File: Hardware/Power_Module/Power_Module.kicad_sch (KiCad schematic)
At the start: 0 parts

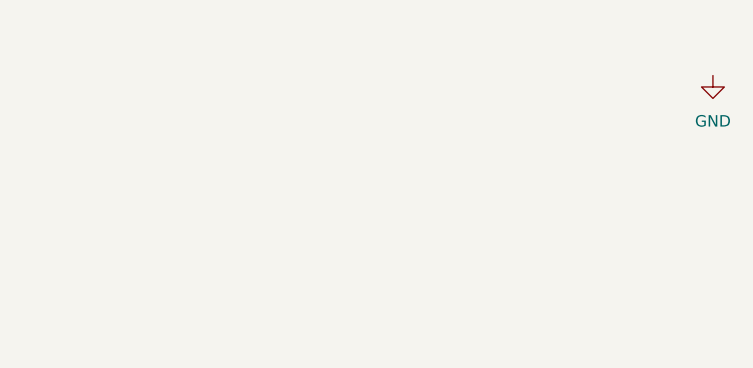
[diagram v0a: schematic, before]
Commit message: added powermodule ic
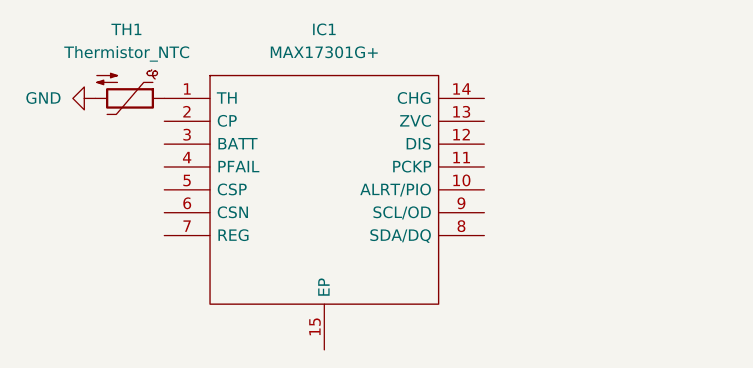
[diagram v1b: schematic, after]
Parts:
- added IC1: MAX17301G+, SON40P300X300X80-15N, symbol MAX17301G+:MAX17301G+
- added TH1: Thermistor_NTC, symbol Device:Thermistor_NTC
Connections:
- net GND: now also TH1.2
- new net: IC1.1 (TH), TH1.1
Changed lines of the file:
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@@
 (kicad_sch
-	(version 20231120)
+	(version 20250114)
 	(generator "eeschema")
-	(generator_version "8.0")
+	(generator_version "9.0")
 	(paper "A4")
 	(symbol
+		(lib_id "MAX17301G+:MAX17301G+")
+		(at 133.35 100.33 0)
+		(unit 1)
+		(exclude_from_sim no)
+		(in_bom yes)
+		(on_board yes)
+		(dnp no)
+		(fields_autoplaced yes)
+		(property "Reference" "IC1"
+			(at 151.13 92.71 0)
+			(effects
+				(font
+					(size 1.27 1.27)
+				)
+			)
+		)
+		(property "Value" "MAX17301G+"
+			(at 151.13 95.25 0)
+			(effects
+				(font
+					(size 1.27 1.27)
+				)
+			)
+		)
+		(property "Footprint" "SON40P300X300X80-15N"
+			(at 165.1 97.79 0)
+			(effects
+				(font
+					(size 1.27 1.27)
+				)
+				(justify left)
+				(hide yes)
+			)
+		)
+		(property "Datasheet" "https://www.analog.com/MAX17301/datasheet"
+			(at 165.1 100.33 0)
+			(effects
+				(font
+					(size 1.27 1.27)
+				)
+				(justify left)
+				(hide yes)
+			)
+		)
+		(property "Description" "1-Cell ModelGauge m5 EZ Fuel Gauge with Protector, Internal Self-Discharge Detection and SHA-256 Authentication"
+			(at 133.35 100.33 0)
+			(effects
+				(font
+					(size 1.27 1.27)
+				)
+				(hide yes)
+			)
+		)
+		(property "Description_1" "1-Cell ModelGauge m5 EZ Fuel Gauge with Protector, Internal Self-Discharge Detection and SHA-256 Authentication"
+			(at 165.1 102.87 0)
+			(effects
+				(font
+					(size 1.27 1.27)
+				)
+				(justify left)
+				(hide yes)
+			)
+		)
+		(property "Height" "0.8"
+			(at 165.1 105.41 0)
+			(effects
+				(font
+					(size 1.27 1.27)
+				)
+				(justify left)
+				(hide yes)
+			)
+		)
+		(property "Mouser Part Number" "700-MAX17301G+"
+			(at 165.1 107.95 0)
+			(effects
+				(font
+					(size 1.27 1.27)
+				)
+				(justify left)
+				(hide yes)
+			)
+		)
+		(property "Mouser Price/Stock" "https://www.mouser.co.uk/ProductDetail/Analog-Devices-Maxim-Integrated/MAX17301G%2b?qs=Wj%2FVkw3K%252BMADpZZVIAh9Qg%3D%3D"
+			(at 165.1 110.49 0)
+			(effects
+				(font
+					(size 1.27 1.27)
+				)
+				(justify left)
+				(hide yes)
+			)
+		)
+		(property "Manufacturer_Name" "Analog Devices"
+			(at 165.1 113.03 0)
+			(effects
+				(font
+					(size 1.27 1.27)
+				)
+				(justify left)
+				(hide yes)
+			)
+		)
+		(property "Manufacturer_Part_Number" "MAX17301G+"
+			(at 165.1 115.57 0)
+			(effects
+				(font
+					(size 1.27 1.27)
+				)
+				(justify left)
+				(hide yes)
+			)
+		)
+		(pin "6"
+		)
+		(pin "5"
+		)
+		(pin "15"
+		)
+		(pin "2"
+		)
+		(pin "13"
+		)
+		(pin "10"
+		)
+		(pin "12"
+		)
+		(pin "7"
+		)
+		(pin "9"
+		)
+		(pin "3"
+		)
+		(pin "14"
+		)
+		(pin "4"
+		)
+		(pin "8"
+		)
+		(pin "1"
+		)
+		(pin "11"
+		)
+		(instances
+			(project ""
+				(path "/48054948-0b09-404e-8bb9-61684bc2977f"
+					(reference "IC1")
+					(unit 1)
+				)
+			)
+		)
+	)
+	(symbol
 		(lib_id "power:GND")
-		(at 194.31 97.79 0)
+		(at 125.73 100.33 270)
 		(unit 1)
 		(exclude_from_sim no)
@@
 		(fields_autoplaced yes)
 		(property "Reference" "#PWR01"
-			(at 194.31 104.14 0)
+			(at 119.38 100.33 0)
 			(effects
 				(font
@@
 		)
 		(property "Value" "GND"
-			(at 194.31 102.87 0)
-			(effects
-				(font
-					(size 1.27 1.27)
-				)
+			(at 121.92 100.3299 90)
+			(effects
+				(font
+					(size 1.27 1.27)
+				)
+				(justify right)
 			)
 		)
 		(property "Footprint" ""
-			(at 194.31 97.79 0)
+			(at 125.73 100.33 0)
 			(effects
 				(font
@@
 		)
 		(property "Datasheet" ""
-			(at 194.31 97.79 0)
+			(at 125.73 100.33 0)
 			(effects
 				(font
@@
 		)
 		(property "Description" "Power symbol creates a global label with name \"GND\" , ground"
-			(at 194.31 97.79 0)
+			(at 125.73 100.33 0)
 			(effects
 				(font
@@
 		)
 	)
+	(symbol
+		(lib_id "Device:Thermistor_NTC")
+		(at 129.54 100.33 270)
+		(unit 1)
+		(exclude_from_sim no)
+		(in_bom yes)
+		(on_board yes)
+		(dnp no)
+		(fields_autoplaced yes)
+		(property "Reference" "TH1"
+			(at 129.2225 92.71 90)
+			(effects
+				(font
+					(size 1.27 1.27)
+				)
+			)
+		)
+		(property "Value" "Thermistor_NTC"
+			(at 129.2225 95.25 90)
+			(effects
+				(font
+					(size 1.27 1.27)
+				)
+			)
+		)
+		(property "Footprint" ""
+			(at 130.81 100.33 0)
+			(effects
+				(font
+					(size 1.27 1.27)
+				)
+				(hide yes)
+			)
+		)
+		(property "Datasheet" "~"
+			(at 130.81 100.33 0)
+			(effects
+				(font
+					(size 1.27 1.27)
+				)
+				(hide yes)
+			)
+		)
+		(property "Description" "Temperature dependent resistor, negative temperature coefficient"
+			(at 129.54 100.33 0)
+			(effects
+				(font
+					(size 1.27 1.27)
+				)
+				(hide yes)
+			)
+		)
+		(pin "1"
+		)
+		(pin "2"
+		)
+		(instances
+			(project ""
+				(path "/48054948-0b09-404e-8bb9-61684bc2977f"
+					(reference "TH1")
+					(unit 1)
+				)
+			)
+		)
+	)
 	(sheet_instances
 		(path "/"
@@
 		)
 	)
+	(embedded_fonts no)
 )

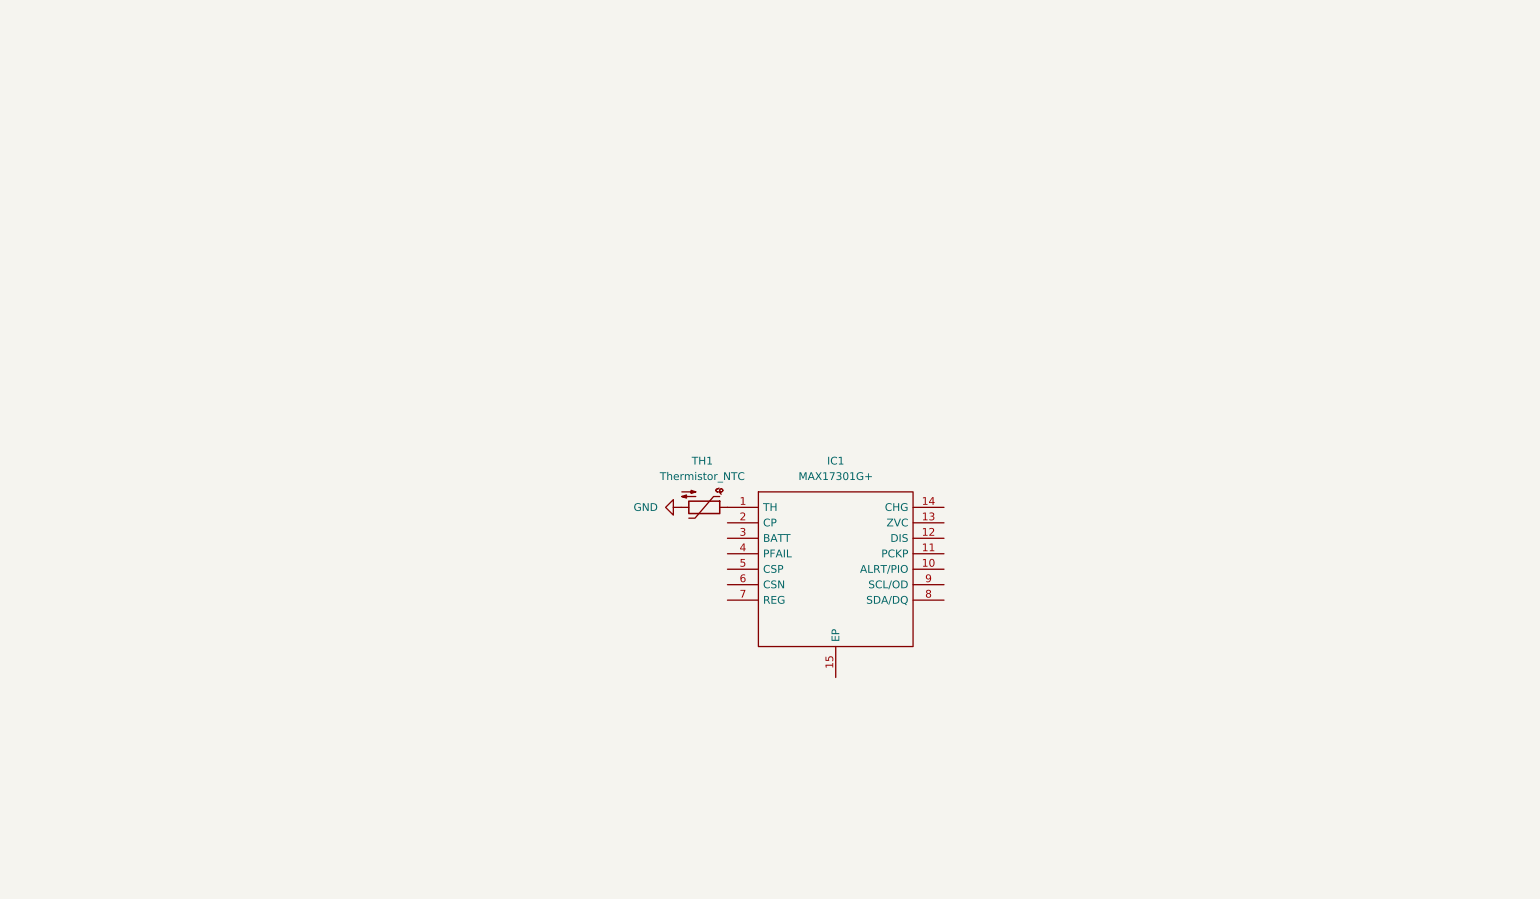
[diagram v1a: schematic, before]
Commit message: Added power module pcb
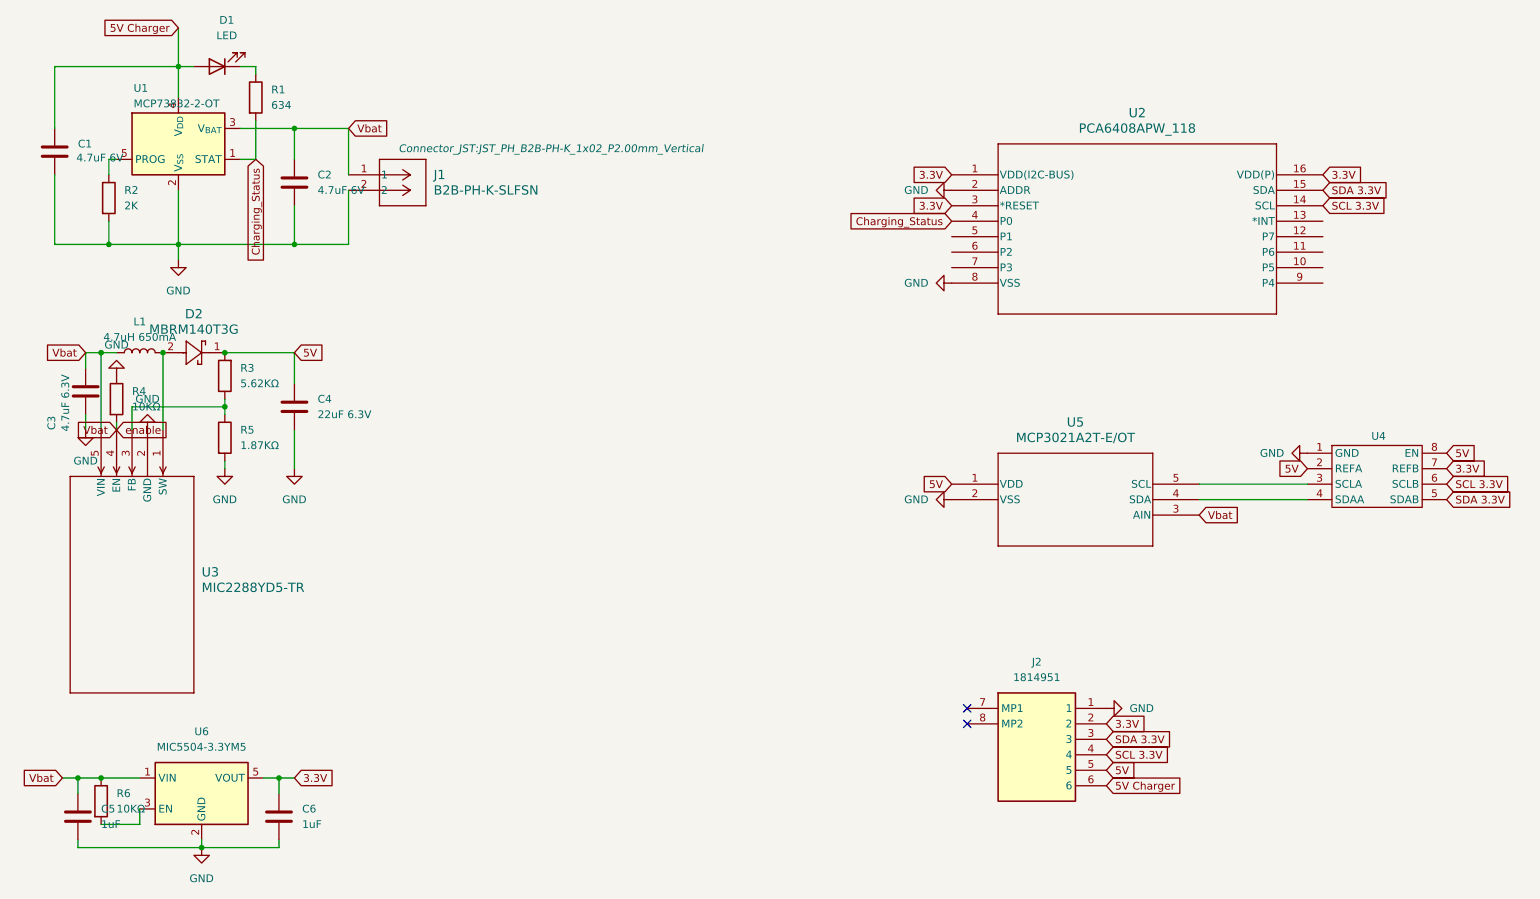
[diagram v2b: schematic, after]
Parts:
- removed IC1: MAX17301G+, SON40P300X300X80-15N, symbol MAX17301G+:MAX17301G+
- removed TH1: Thermistor_NTC, symbol Device:Thermistor_NTC
- added C1, C2: 4.7uF 6V, Capacitor_SMD:C_1206_3216Metric, symbol Device:C
- added C3: 4.7uF 6.3V, Capacitor_SMD:C_0805_2012Metric, symbol Device:C
- added C4: 22uF 6.3V, Capacitor_SMD:C_0805_2012Metric, symbol Device:C
- added C5, C6: 1uF, Capacitor_SMD:C_0402_1005Metric, symbol Device:C
- added D1: LED, LED_SMD:LED_0402_1005Metric, symbol Device:LED
- added D2: MBRM140T3G, Diode_SMD:D_SOD-123, symbol 2025-05-15_08-50-35:MBRM140T3G
- added J1: B2B-PH-K-SLFSN, Connector_JST:JST_PH_B2B-PH-K_1x02_P2.00mm_Vertical, symbol 2025-05-14_09-03-17:B2B-PH-K-SLFSN
- added J2: 1814951, footprints:1814951, symbol connectors_ptms:1814951
- added L1: 4.7uH 650mA, Capacitor_SMD:C_1210_3225Metric, symbol Device:L
- added R1: 634, Capacitor_SMD:C_0402_1005Metric, symbol Device:R
- added R2: 2K, Resistor_SMD:R_0402_1005Metric, symbol Device:R
- added R3: 5.62KΩ, Resistor_SMD:R_0603_1608Metric, symbol Device:R
- added R4, R6: 10KΩ, Resistor_SMD:R_0603_1608Metric, symbol Device:R
- added R5: 1.87KΩ, Resistor_SMD:R_0603_1608Metric, symbol Device:R
- added U1: MCP73832-2-OT, Package_TO_SOT_SMD:SOT-23-5, symbol Battery_Management:MCP73832-2-OT
- added U2: PCA6408APW_118, Package_SO:TSSOP-16_4.4x5mm_P0.65mm, symbol 2025-05-14_11-29-24:PCA6408APW_118
- added U3: MIC2288YD5-TR, Package_TO_SOT_SMD:TSOT-23-5, symbol 2025-05-14_10-11-59:MIC2288YD5-TR
- added U4: ~, Package_SO:TSSOP-8_3x3mm_P0.65mm, symbol Level_Shifter:_NCA9306
- added U5: MCP3021A2T-E/OT, Package_TO_SOT_SMD:TSOT-23-5, symbol 2025-05-14_12-06-52:MCP3021A2T-E_OT
- added U6: MIC5504-3.3YM5, Package_TO_SOT_SMD:SOT-23-5, symbol Regulator_Linear:MIC5504-3.3YM5
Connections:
- net GND: now also C1.2, C2.2, C3.2, C4.2, C5.2, C6.2, J1.2, J2.1, R2.2, R4.1, R5.2, U1.2 (V_{SS}), U2.2 (ADDR), U2.8 (VSS), U3.2 (GND), U4.1 (GND), U5.2 (VSS), U6.2 (GND)
- new net: U4.4 (SDAA), U5.4 (SDA)
- new net: U4.3 (SCLA), U5.5 (SCL)
- new net: R3.1, R5.1, U3.3 (FB)
- new net: R2.1, U1.5 (PROG)
- new net: R6.2, U6.3 (EN)
- new net: D2.2, L1.2, U3.1 (SW)
- new net: D1.1 (K), R1.1
- new net 3.3V: C6.1, J2.2, U2.1 (VDD(I2C-BUS)), U2.16 (VDD(P)), U2.3 (*RESET), U4.7 (REFB), U6.5 (VOUT)
- new net 5V: C4.1, D2.1, J2.5, R3.2, U4.2 (REFA), U4.8 (EN), U5.1 (VDD)
- new net 5V Charger: C1.1, D1.2 (A), J2.6, U1.4 (V_{DD})
- new net Charging_Status: R1.2, U1.1 (STAT), U2.4 (P0)
- new net SCL 3.3V: J2.4, U2.14 (SCL), U4.6 (SCLB)
- new net SDA 3.3V: J2.3, U2.15 (SDA), U4.5 (SDAB)
- new net Vbat: C2.1, C3.1, C5.1, J1.1, L1.1, R4.2, R6.1, U1.3 (V_{BAT}), U3.4 (EN), U3.5 (VIN), U5.3 (AIN), U6.1 (VIN)
- no-connect marks 0 -> 2

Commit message: Added LED Matrix for fun
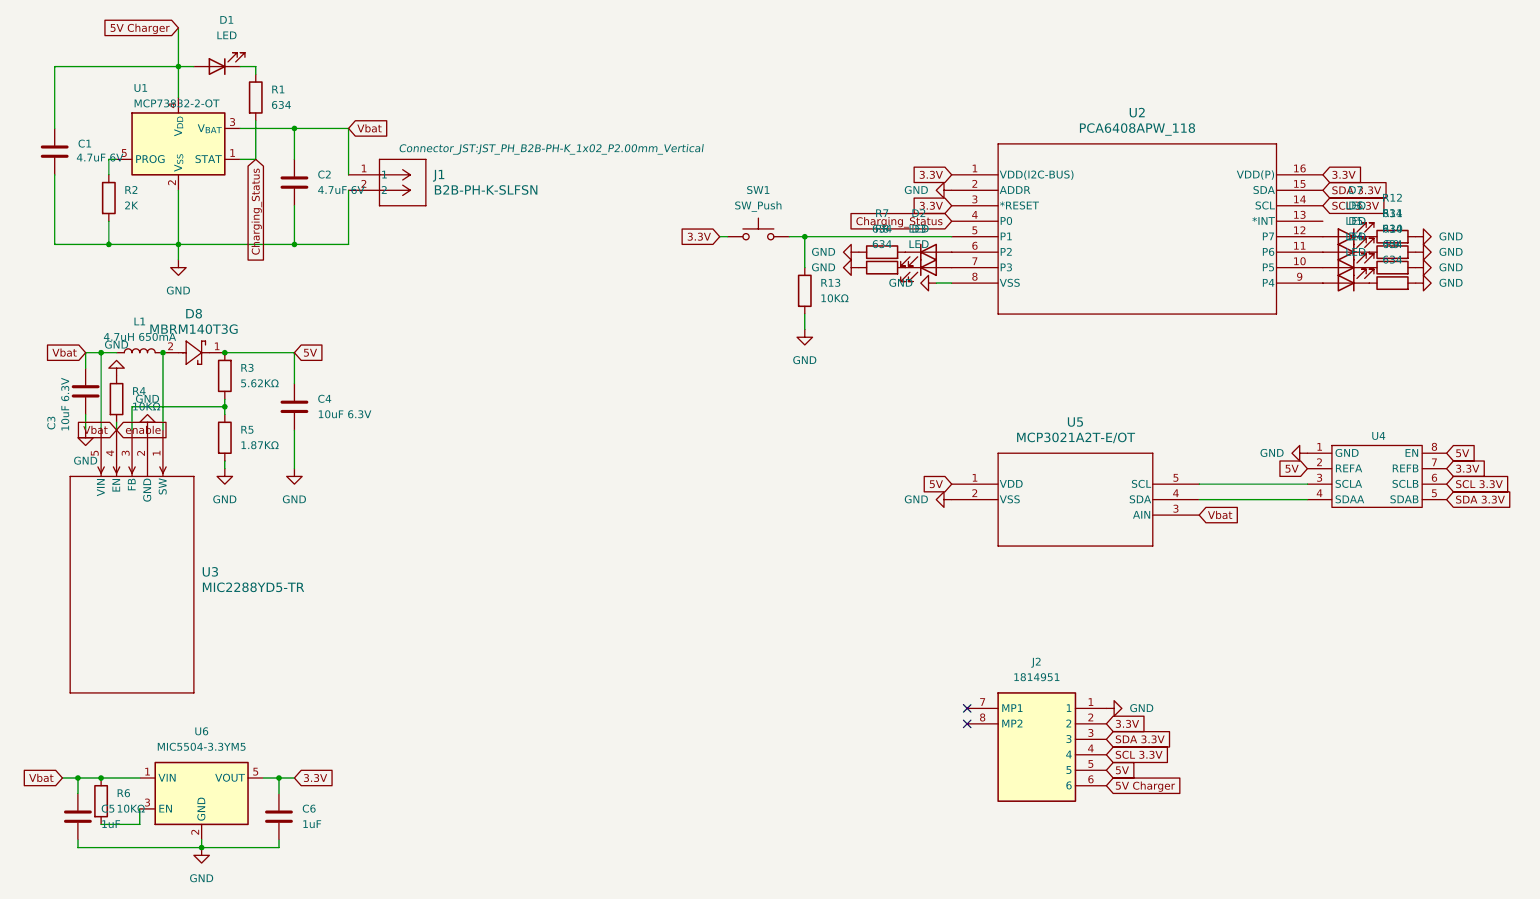
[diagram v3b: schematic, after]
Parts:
- added D2, D3, D4, D5, D6, D7: LED, LED_SMD:LED_0402_1005Metric, symbol Device:LED
- added R10, R11, R12, R7, R8, R9: 634, Capacitor_SMD:C_0402_1005Metric, symbol Device:R
- added R13: 10KΩ, Resistor_SMD:R_0603_1608Metric, symbol Device:R
- added SW1: SW_Push, Button_Switch_SMD:SW_Tactile_SPST_NO_Straight_CK_PTS636Sx25SMTRLFS, symbol Switch:SW_Push
- C3: value 4.7uF 6.3V -> 10uF 6.3V
- C4: value 22uF 6.3V -> 10uF 6.3V
- J2: footprint footprints:1814951 -> Library:1814951
- renumbered D2 to D8
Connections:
- net 3.3V: now also SW1.1
- net GND: now also R10.2, R11.2, R12.2, R13.2, R7.1, R8.1, R9.2
- net at U2.10 (P5): now also D5.2 (A)
- net at U2.11 (P6): now also D6.2 (A)
- net at U2.12 (P7): now also D7.2 (A)
- net at U2.5 (P1): now also R13.1, SW1.2
- net at U2.6 (P2): now also D2.2 (A)
- net at U2.7 (P3): now also D3.2 (A)
- net at U2.9 (P4): now also D4.2 (A)
- new net: D5.1 (K), R10.1
- new net: D7.1 (K), R12.1
- new net: D2.1 (K), R7.2
- new net: D6.1 (K), R11.1
- new net: D4.1 (K), R9.1
- new net: D3.1 (K), R8.2
